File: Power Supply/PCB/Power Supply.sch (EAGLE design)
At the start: 39 parts, among them IC1 LM741P, IC2 LM741P, IC3 LM741P

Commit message: Power supply PCB still in progress
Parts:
- added U$37, U$56, U$64: 100uF/50V, Capstone:100UF
- added U$38, U$57, U$58, U$65: 0.1uF/50V, Capstone:CERAMIC_CAPACITOR
- added U$39, U$45: 12V, Capstone:1W_ZENER
- added U$40, U$46: 500 OHM/0.5W, Capstone:0.5W_RES
- added U$41, U$42, U$47, U$48, U$60: 10k, Capstone:0.25W_RES
- added U$43, U$44, U$62, U$69: 1uF/50V, Capstone:CERAMIC_CAPACITOR
- added U$49: (no value), Capstone:1N4005
- added U$50: 220uF/50V, Capstone:220UF
- added U$51: 1K/0.5W, Capstone:0.5W_RES
- added U$52, U$53: (no value), Capstone:2N4403
- added U$54: 10k, Capstone:10K_TRIMMER
- added U$55: 5k, Capstone:0.25W_RES
- added U$59: (no value), Capstone:10K_TRIMMER
- added U$61: 5.1V, Capstone:1W_ZENER
- added U$63: 2N4401, Capstone:2N4401
- added U$66: (no value), Capstone:THYRISTOR_4A
- added U$67: 6.2V, Capstone:1W_ZENER
- added U$68: 100 OHM, Capstone:0.25W_RES
- added U$70, U$71: P6KE15A-E3/54GICT-ND_TVS_DIODE, TVS Diode Through-Hole:P6KE15A-E3/54GICT-ND_TVS_DIODE
- U$10: value (none) -> 10 OHM/5W
- U$11: value (none) -> 1 OHM/5W
- U$16: value (none) -> 10000uF/16V
- U$30: value (none) -> 100uF/50V; device Capstone:220UF -> Capstone:100UF
- U$35: value (none) -> 10k
- U$36: value (none) -> 5k
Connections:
- new net +12V: IC3.V+, U$3.E, U$36.2, U$37.+, U$38.1
- new net +12V_FEEDBACK: IC1.-IN, U$35.E, U$36.1
- new net +12V_REF: IC1.+IN, U$41.2, U$42.1
- new net +5V: U$1.E, U$59.E, U$64.+, U$65.1, U$67.C
- new net +5V_FEEDBACK: IC3.-IN, U$59.S
- new net -12V: IC3.V-, U$2.E, U$55.1, U$56.-, U$57.2
- new net -12V_FEEDBACK: IC2.-IN, U$54.S, U$55.2
- new net -12V_REF: IC2.+IN, U$47.1, U$48.2
- new net N$15: U$39.C, U$40.1, U$42.2, U$43.1
- new net N$16: U$49.A, U$50.-, U$51.1, U$52.C
- new net N$17: IC3.+IN, U$60.1, U$61.C, U$62.1
- new net N$18: U$44.2, U$45.A, U$46.2, U$48.1
- new net N$19: U$12.2, U$17.1
- new net N$20: U$30.-, U$51.2, U$52.B
- new net N$21: IC2.V-, U$52.E
- new net N$23: U$10.2, U$2.C, U$53.C
- new net N$24: U$2.B, U$53.E
- new net N$25: IC2.OUT, U$53.B
- new net N$26: U$1.C, U$11.2, U$63.C
- new net N$27: U$12.1, U$24.A, U$25.C
- new net N$28: IC3.OUT, U$63.B
- new net N$29: U$22.C, U$24.C, U$7.1
- new net N$30: U$11.1, U$16.+, U$58.1, U$60.2, U$7.2
- new net N$32: U$1.B, U$63.E
- new net N$33: U$66.G, U$67.A, U$68.2, U$69.1
- new net OV_THYRISTOR: U$17.2, U$22.A, U$23.C, U$66.A
- net GND: now also IC2.V+, U$16.-, U$23.A, U$25.A, U$30.+, U$35.S, U$37.-, U$38.2, U$39.A, U$41.1, U$43.2, U$44.1, U$45.C, U$47.2, U$50.+, U$54.E, U$56.+, U$57.1, U$58.2, U$59.A, U$61.A, U$62.2, U$64.-, U$65.2, U$66.C, U$68.1, U$69.2
- net N$1: now also U$6.1; no longer U$14.1
- net N$2: now also U$14.2; no longer U$13.3
- net N$3: now also U$15.2; no longer U$13.1
- net N$4: now also U$8.1; no longer U$15.1
- net N$5: now also U$13.3, U$14.1; no longer U$14.2, U$6.1
- net N$6: now also U$13.1, U$15.1; no longer U$15.2, U$8.1
- net N$7: now also U$40.2
- net N$9: now also U$10.1, U$46.1, U$49.C
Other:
- moved on the sheet: IC1, IC2, IC3, U$1, U$10, U$11, U$12, U$13, U$14, U$15, U$16, U$17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

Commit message: Finished PCB
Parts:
- removed U$70, U$71: P6KE15A-E3/54GICT-ND_TVS_DIODE, TVS Diode Through-Hole:P6KE15A-E3/54GICT-ND_TVS_DIODE
- added GND: M3_SCREW_TERMINAL, EcoCar Temp:M3_SCREW_TERMINAL
- added H1, H2, H3, H4: STAND-OFF, SparkFun-Hardware:STAND-OFF
- added POWER_1, POWER_2, POWER_3, POWER_4, POWER_5, POWER_6, POWER_7: TE-6PIN, Capstone:TE-6PIN
- IC1, IC2, IC3: value LM741P -> LM741; device linear:LM741P -> Capstone:LM741
- renumbered U$1 to Q8, U$10 to R11, U$11 to R14, U$12 to 6.3V, U$13 to 33V, U$14 to F1, U$15 to F2, U$16 to C6, U$17 to F3, U$18 to D1, U$19 to D2, U$2 to Q6, U$20 to D3, U$21 to D4, U$22 to D5, U$23 to D6, U$24 to D7, U$25 to D8, U$26 to C1, U$27 to C2, U$28 to D10, U$29 to C8, U$3 to Q3, U$30 to C14, U$31 to C9, U$32 to R5, U$33 to Q1, U$34 to Q2, U$35 to TRIM1, U$36 to R6, U$37 to C10, U$38 to C11, U$39 to D9, U$4 to C3, U$40 to R1, U$41 to R3, U$42 to R2, U$43 to C7, U$44 to C12, U$45 to D11, U$46 to R9, U$47 to R7, U$48 to R8, U$49 to D12, U$5 to C4, U$50 to C13, U$51 to R10, U$52 to Q4, U$53 to Q5, U$54 to TRIM2, U$55 to R12, U$56 to C15, U$57 to C16, U$58 to C5, U$59 to TRIM3, U$6 to L1, U$60 to R13, U$61 to D13, U$62 to C17, U$63 to Q7, U$64 to C18, U$65 to C19, U$66 to SCR1, U$67 to D14, U$68 to R15, U$69 to C20, U$7 to L3, U$8 to L2, U$9 to R4
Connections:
- net +12V: now also POWER_1.2, POWER_2.2, POWER_3.2, POWER_4.2, POWER_5.2, POWER_6.2, POWER_7.2
- net +5V: now also POWER_1.6, POWER_2.6, POWER_3.6, POWER_4.6, POWER_5.6, POWER_6.6, POWER_7.6
- net -12V: now also POWER_1.4, POWER_2.4, POWER_3.4, POWER_4.4, POWER_5.4, POWER_6.4, POWER_7.4
- net GND: now also GND.1, GND.2, GND.3, GND.4, POWER_1.1, POWER_1.3, POWER_1.5, POWER_2.1, POWER_2.3, POWER_2.5, POWER_3.1, POWER_3.3, POWER_3.5, POWER_4.1, POWER_4.3, POWER_4.5, POWER_5.1, POWER_5.3, POWER_5.5, POWER_6.1, POWER_6.3, POWER_6.5, POWER_7.1, POWER_7.3, POWER_7.5

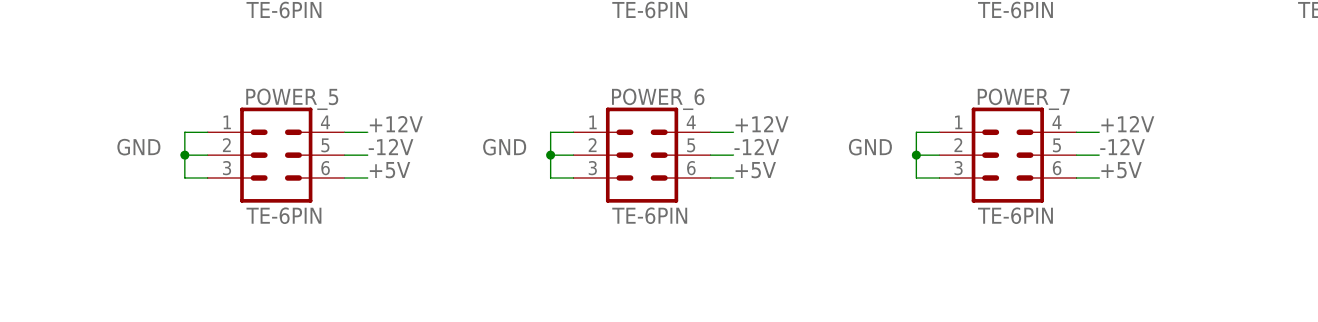
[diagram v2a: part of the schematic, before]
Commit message: Added note to clarify analog and digital ground
Added note to clarify analog and digital ground. Pin 3 is digital, 1 & 2 are analog.
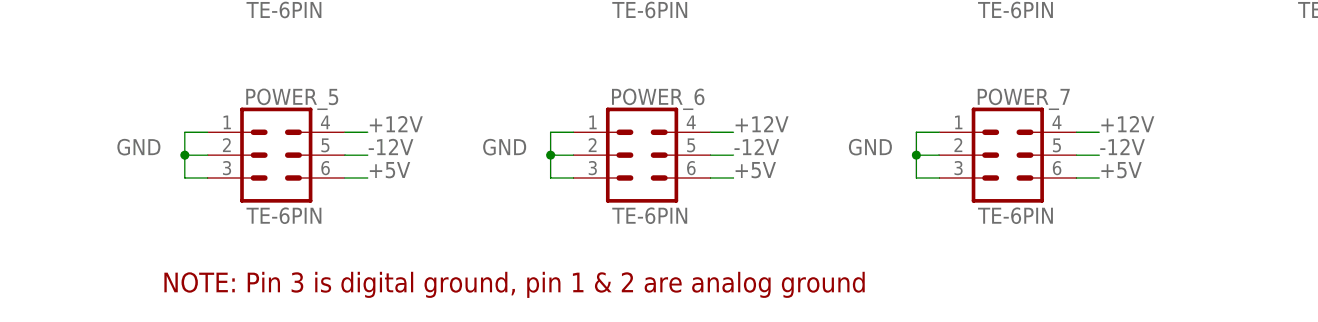
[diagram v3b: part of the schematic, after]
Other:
- note added: "NOTE: Pin 3 is digital ground, pin 1 & 2 are analog ground"
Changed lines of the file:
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@@
 <?xml version="1.0" encoding="utf-8"?>
 <!DOCTYPE eagle SYSTEM "eagle.dtd">
-<eagle version="9.2.2">
+<eagle version="8.6.2">
 <drawing>
 <settings>
@@
 <sheet>
 <plain>
+<text x="78.74" y="22.86" size="2.1844" layer="94">NOTE: Pin 3 is digital ground, pin 1 &amp; 2 are analog ground</text>
 </plain>
 <instances>

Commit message: updated schematic
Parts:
- D1, D10, D12, D2, D3, D4, D5, D6, D7, D8: value (none) -> 1N4005
- D13: value 5.1V -> 3.3V
- F1, F2: value (none) -> 500mA Slow Blow
- F3: value (none) -> 750mA Slow Blow
- Q1, Q2: value (none) -> 2N4401
- Q4, Q5: value (none) -> 2N4403
- R13: value 10k -> 100
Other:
- note added: "NOTE: Pin 3 is digital ground, pin 1 & 2 are analog ground (they are separated in the board layout)"
- note removed: "NOTE: Pin 3 is digital ground, pin 1 & 2 are analog ground"
